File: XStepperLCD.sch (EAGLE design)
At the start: 43 parts, among them Q2 16 MHZ, U1 LCD-16X2NOHOLES

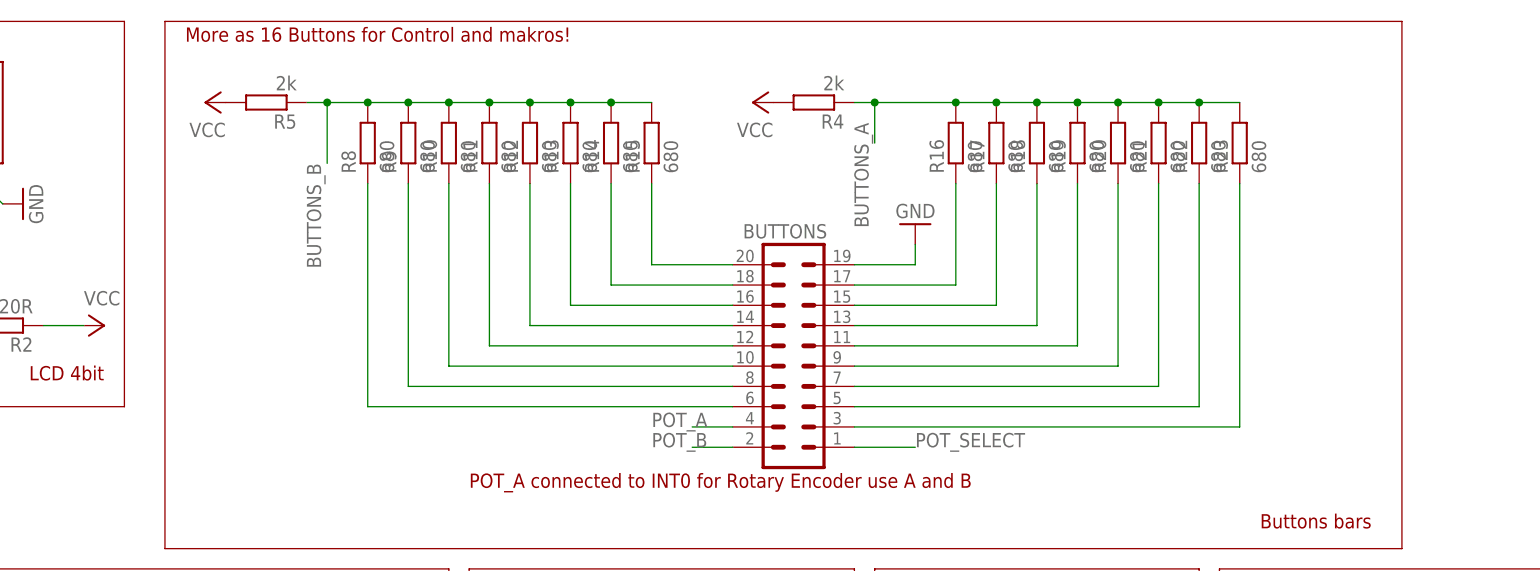
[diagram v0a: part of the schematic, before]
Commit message: - bugfic: set all buttons resistor to different values
- fix schema and board
- fix some typos and bugs in readButtons
- add thread to read buttons
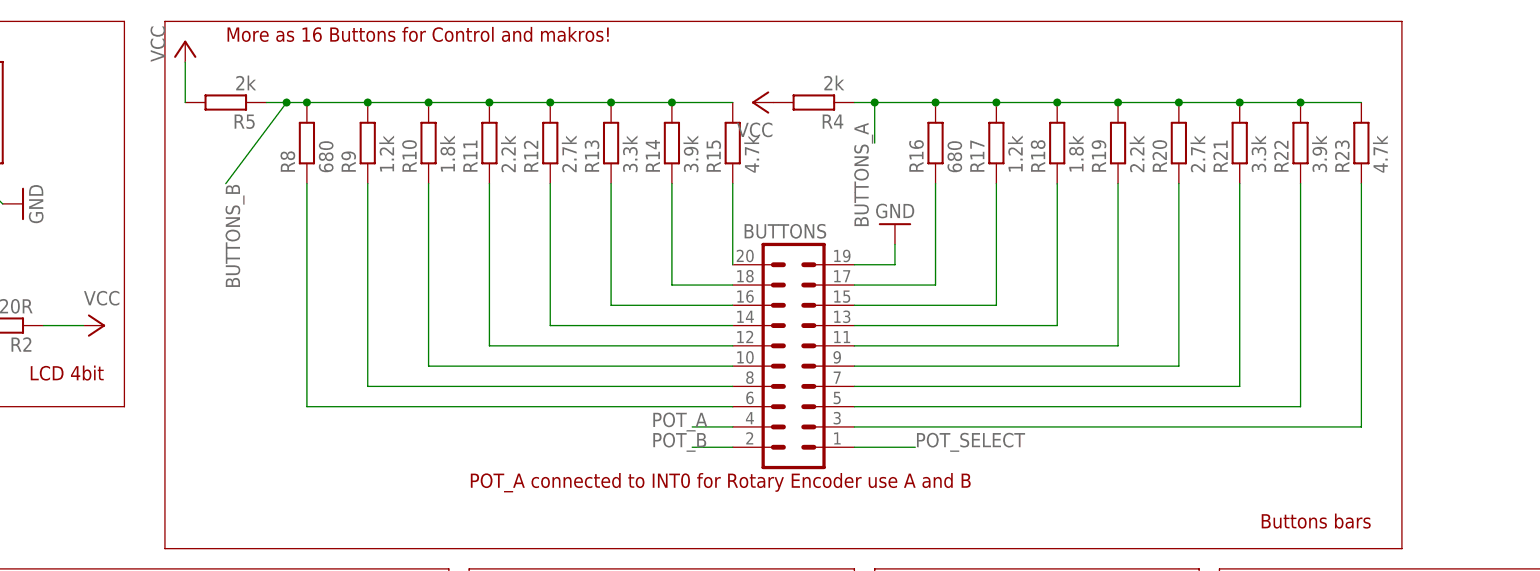
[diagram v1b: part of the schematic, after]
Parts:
- R10, R18: value 680 -> 1.8k
- R11, R19: value 680 -> 2.2k
- R12, R20: value 680 -> 2.7k
- R13, R21: value 680 -> 3.3k
- R14, R22: value 680 -> 3.9k
- R15, R23: value 680 -> 4.7k
- R17, R9: value 680 -> 1.2k
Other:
- moved on the sheet: R10, R12, R13, R14, R15, R16, R18, R19, R20, R21, R22, R23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

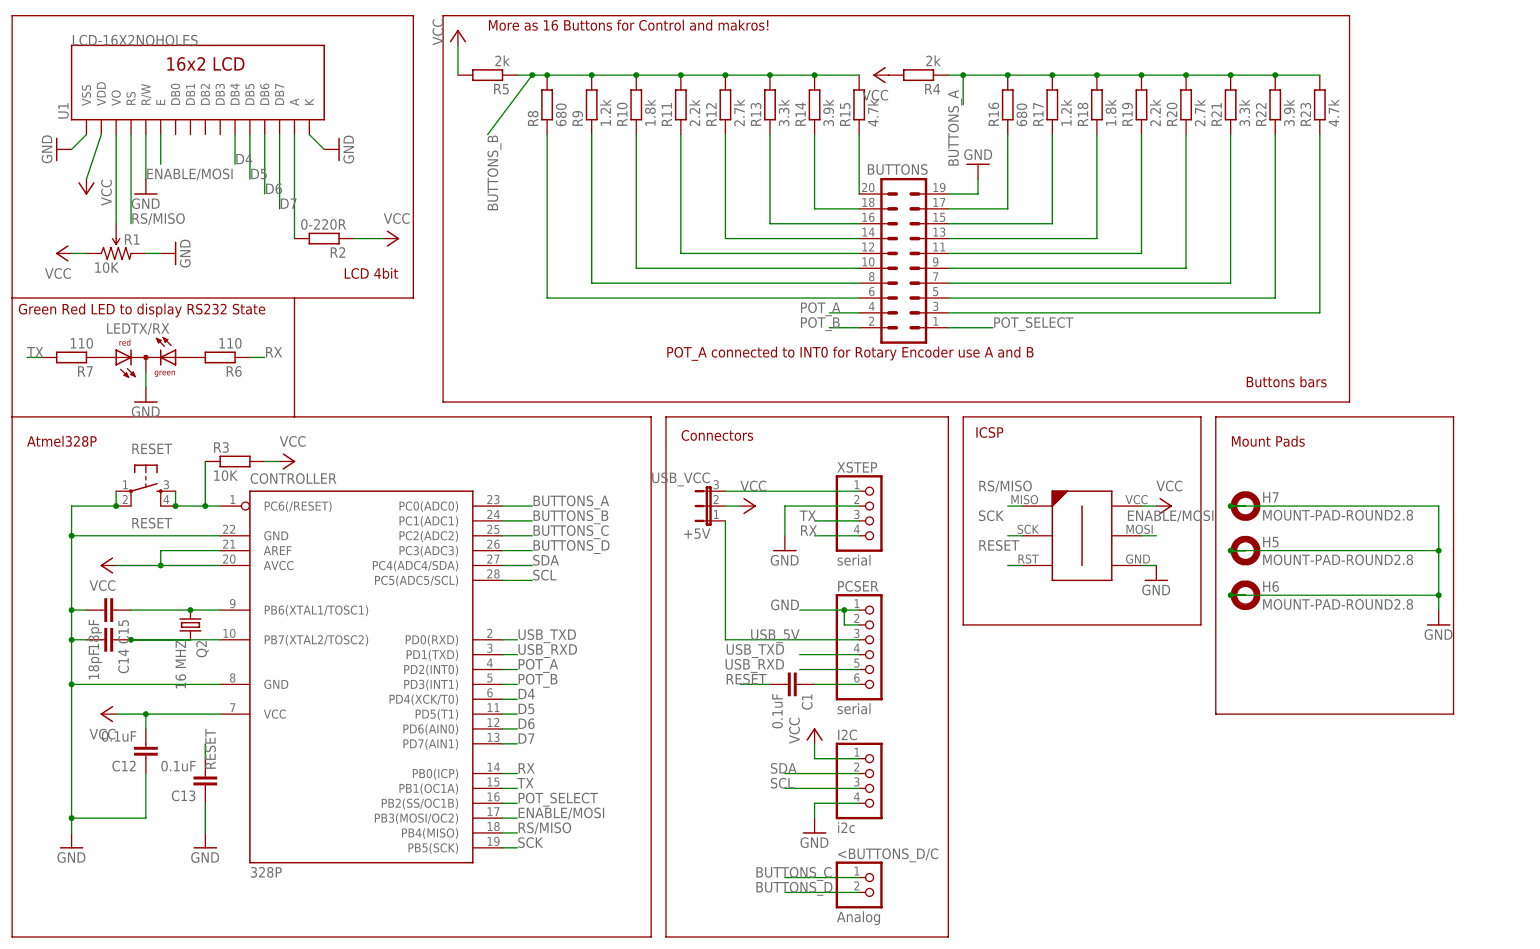
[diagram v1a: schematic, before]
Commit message: - replace some TH parts with SMD and bugfixes
- remove reset button
- remove power pin and choose only power from xstepper
- add RJ45 plugin for connect XStepper
- change all button resistors to 680r and connect serial
- remove LED from serial line and put a new one to A7
- add some text to I2C
- change Atmega328 to SMD Version
- change Quartz to SMD ceramic resonator (16MHz)
- replace ICSP to normal 2x3 pin header
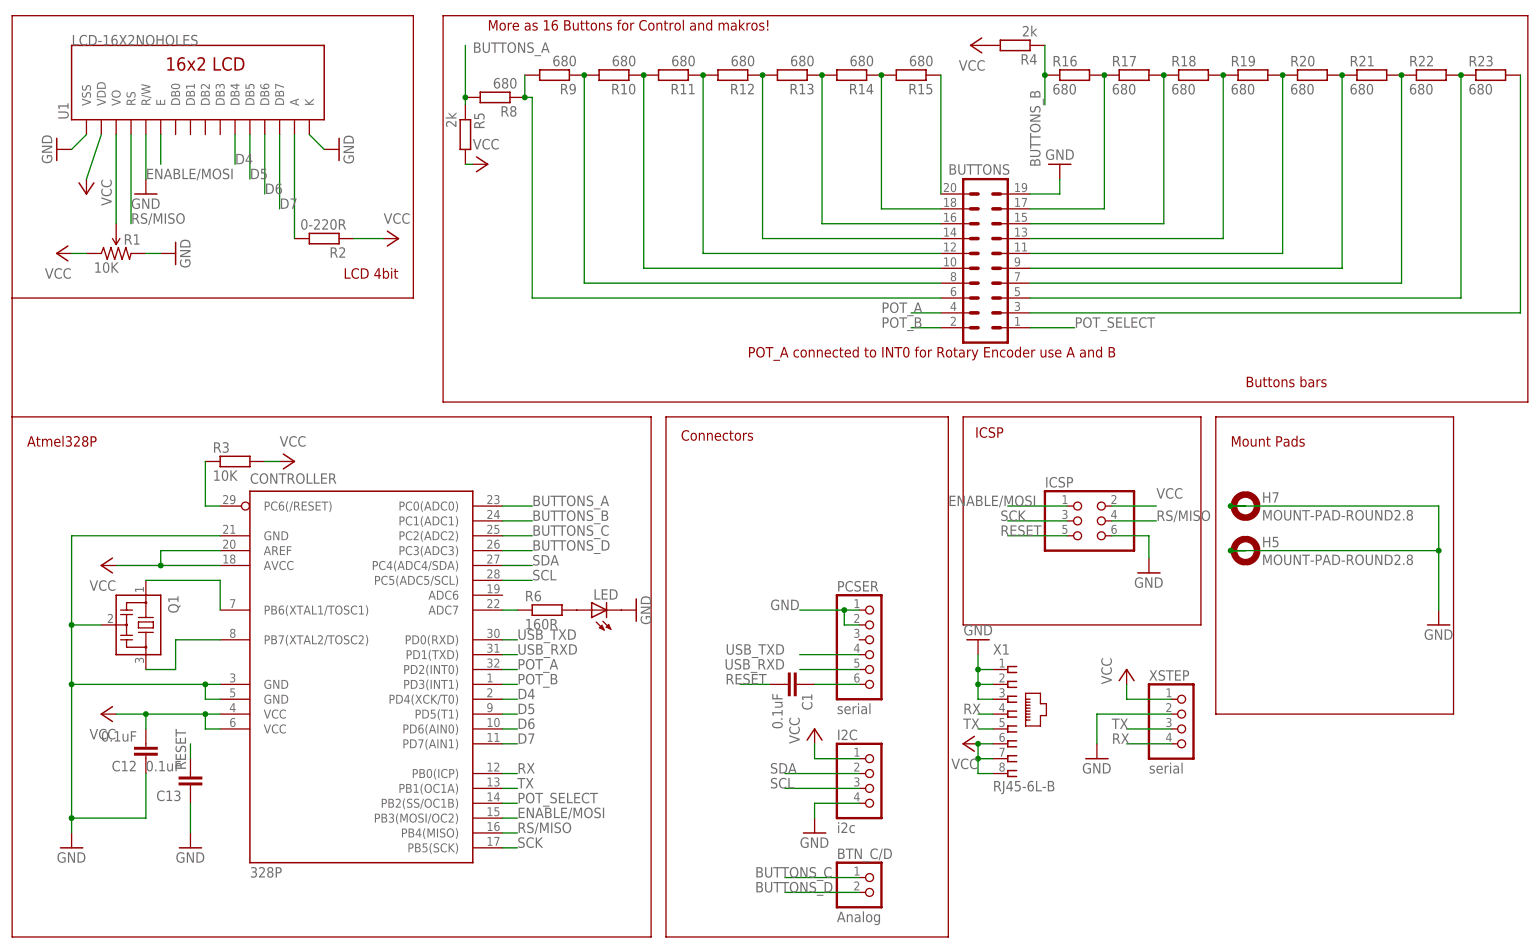
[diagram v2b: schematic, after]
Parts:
- removed +5V: USB_VCC, jumper:JP2E
- removed C14, C15: 18pF, resistor:C-EUC1206
- removed H6: MOUNT-PAD-ROUND2.8, holes:MOUNT-PAD-ROUND2.8
- removed LEDTX/RX: (no value), led:DUOLED2X5
- removed Q2: 16 MHZ, crystal:CRYSTALHC49S
- removed R7: 110, resistor:R-EU_R1206
- removed RESET: RESET, SparkFun:TAC_SWITCHSMD
- added LED: (no value), led:LEDSMT1206
- added Q1: CSTCR6M00G53Z, murata-filter:CSTCR6M00G53Z
- added X1: RJ45-6L-B, con-tycoelectronics:RJ45-6L-B
- 328P: device Bibsatmel:MEGA8-P -> atmel:MEGA8-AI
- ICSP: value ICSP -> (none); device avr-7:AVR-ISP-6-EDGE -> pinhead:PINHD-2X3
- R10, R18: value 1.8k -> 680
- R11, R19: value 2.2k -> 680
- R12, R20: value 2.7k -> 680
- R13, R21: value 3.3k -> 680
- R14, R22: value 3.9k -> 680
- R15, R23: value 4.7k -> 680
- R17, R9: value 1.2k -> 680
- R6: value 110 -> 160R
- renumbered <BUTTONS_D/C to BTN_C/D
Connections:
- removed net N$12 (its old number): BUTTONS.12, R11.1
- removed net N$16: BUTTONS.7, R21.1
- removed net N$17: BUTTONS.9, R20.1
- removed net N$18: BUTTONS.11, R19.1
- removed net N$19: BUTTONS.18, R14.1
- removed net N$21: LEDTX/RX.AG, R6.2
- removed net N$22: LEDTX/RX.AR, R7.1
- removed net N$33: 328P.PB6(XTAL1/TOSC1), C15.1, Q2.1
- removed net USB_5V: +5V.1, PCSER.3
- removed net XSTEP_5V: +5V.3, XSTEP.1
- new net N$23: BUTTONS.17, R16.2, R17.1
- new net N$24: BUTTONS.15, R17.2, R18.1
- new net N$25: BUTTONS.13, R18.2, R19.1
- new net N$26: BUTTONS.11, R19.2, R20.1
- new net N$27: BUTTONS.9, R20.2, R21.1
- new net N$28: BUTTONS.7, R21.2, R22.1
- new net N$29: BUTTONS.5, R22.2, R23.1
- new net N$3: 328P.PB6(XTAL1/TOSC1), Q1.1
- net BUTTONS_A: now also R5.1, R8.2; no longer R16.2, R17.2, R18.2, R19.2, R20.2, R21.2, R22.2, R23.2, R4.1
- net BUTTONS_B: now also R16.1, R4.1; no longer R10.2, R11.2, R12.2, R13.2, R14.2, R15.2, R5.1, R8.2, R9.2
- net ENABLE/MOSI: now also ICSP.1; no longer ICSP.P$5
- net GND: now also 328P.GND@2, ICSP.6, LED.C, Q1.2, X1.1, X1.2, X1.3; no longer C14.2, C15.2, H6.MOUNT, ICSP.P$4, LEDTX/RX.C, RESET.1, RESET.2
- net N$10: now also BUTTONS.18, R14.1, R15.2; no longer BUTTONS.5, R22.1
- net N$11: now also BUTTONS.14, R12.1, R13.2; no longer BUTTONS.10, R10.1
- net N$13: now also LED.A, R6.2; no longer BUTTONS.14, R12.1
- net N$15: now also 328P.ADC7, R6.1; no longer BUTTONS.16, R13.1
- net N$34: now also Q1.3; no longer C14.1, Q2.2
- net N$4: now also BUTTONS.3, R23.2; no longer BUTTONS.13, R18.1
- net N$5: now also BUTTONS.6, R8.1, R9.2; no longer BUTTONS.15, R17.1
- net N$6: now also BUTTONS.8, R10.2, R9.1; no longer BUTTONS.17, R16.1
- net N$7: now also BUTTONS.10, R10.1, R11.2; no longer BUTTONS.6, R8.1
- net N$8: now also BUTTONS.12, R11.1, R12.2; no longer BUTTONS.8, R9.1
- net N$9: now also BUTTONS.16, R13.1, R14.2; no longer BUTTONS.3, R23.1
- net RESET: now also ICSP.5; no longer ICSP.P$3, RESET.3, RESET.4
- net RS/MISO: now also ICSP.4; no longer ICSP.P$1
- net RX: now also X1.4; no longer R6.1
- net SCK: now also ICSP.3; no longer ICSP.P$2
- net TX: now also X1.5; no longer R7.2
- net VCC: now also 328P.VCC@2, ICSP.2, X1.6, X1.7, X1.8, XSTEP.1; no longer +5V.2, ICSP.P$6
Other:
- note removed: "Green Red LED to display RS232 State"
- moved on the sheet: BUTTONS, C13, R10, R11, R12, R13, R14, R15, R16, R17, R18, R19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

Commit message: make board bigger
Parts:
- added H1, H2: MOUNT-PAD-ROUND2.8, holes:MOUNT-PAD-ROUND2.8
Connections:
- net BUTTONS_C: now also 328P.ADC6; no longer 328P.PC2(ADC2)
- net BUTTONS_D: now also 328P.ADC7; no longer 328P.PC3(ADC3)
- net ENABLE/MOSI: now also ICSP.4; no longer ICSP.1
- net N$15: now also 328P.PC2(ADC2); no longer 328P.ADC7
- net RS/MISO: now also ICSP.1; no longer ICSP.4
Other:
- moved on the sheet: LED, R6
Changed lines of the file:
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@@
 <?xml version="1.0" encoding="utf-8"?>
 <!DOCTYPE eagle SYSTEM "eagle.dtd">
-<eagle version="6.5.0">
+<eagle version="6.3">
 <drawing>
 <settings>
@@
 <part name="GND11" library="supply1" deviceset="GND" device=""/>
 <part name="P+2" library="supply1" deviceset="VCC" device=""/>
+<part name="H1" library="holes" deviceset="MOUNT-PAD-ROUND" device="2.8" value="MOUNT-PAD-ROUND2.8"/>
+<part name="H2" library="holes" deviceset="MOUNT-PAD-ROUND" device="2.8" value="MOUNT-PAD-ROUND2.8"/>
 </parts>
 <sheets>
@@
 <instance part="GND5" gate="1" x="191.77" y="11.43"/>
 <instance part="Q1" gate="G$1" x="20.32" y="2.54" rot="R270"/>
-<instance part="LED" gate="G$1" x="96.52" y="5.08" rot="R90"/>
-<instance part="GND9" gate="1" x="104.14" y="5.08" rot="R90"/>
-<instance part="R6" gate="G$1" x="88.9" y="5.08"/>
+<instance part="LED" gate="G$1" x="96.52" y="17.78" rot="R90"/>
+<instance part="GND9" gate="1" x="104.14" y="17.78" rot="R90"/>
+<instance part="R6" gate="G$1" x="88.9" y="17.78"/>
 <instance part="X1" gate="G$1" x="167.64" y="-12.7"/>
 <instance part="GND11" gate="1" x="162.56" y="0" rot="R180"/>
 <instance part="P+2" gate="VCC" x="160.02" y="-17.78" rot="R90"/>
+<instance part="H1" gate="G$1" x="208.28" y="7.62"/>
+<instance part="H2" gate="G$1" x="208.28" y="30.48"/>
 </instances>
 <busses>
@@
 <wire x1="205.74" y1="15.24" x2="241.3" y2="15.24" width="0.1524" layer="91"/>
 <wire x1="241.3" y1="15.24" x2="241.3" y2="22.86" width="0.1524" layer="91"/>
-<wire x1="241.3" y1="5.08" x2="241.3" y2="15.24" width="0.1524" layer="91"/>
+<wire x1="241.3" y1="5.08" x2="241.3" y2="7.62" width="0.1524" layer="91"/>
 <junction x="241.3" y="15.24"/>
 <pinref part="GND24" gate="1" pin="GND"/>
@@
 <pinref part="H5" gate="G$1" pin="MOUNT"/>
 <junction x="205.74" y="15.24"/>
+<wire x1="241.3" y1="7.62" x2="241.3" y2="15.24" width="0.1524" layer="91"/>
+<wire x1="208.28" y1="30.48" x2="241.3" y2="30.48" width="0.1524" layer="91"/>
+<wire x1="241.3" y1="30.48" x2="241.3" y2="22.86" width="0.1524" layer="91"/>
+<junction x="241.3" y="22.86"/>
+<wire x1="208.28" y1="7.62" x2="241.3" y2="7.62" width="0.1524" layer="91"/>
+<junction x="241.3" y="7.62"/>
 </segment>
 <segment>
@@
 </segment>
 <segment>
-<pinref part="ICSP" gate="A" pin="4"/>
-<wire x1="185.42" y1="20.32" x2="193.04" y2="20.32" width="0.1524" layer="91"/>
-<label x="193.04" y="20.32" size="1.778" layer="95"/>
+<pinref part="ICSP" gate="A" pin="1"/>
+<wire x1="177.8" y1="22.86" x2="167.64" y2="22.86" width="0.1524" layer="91"/>
+<label x="157.48" y="22.86" size="1.778" layer="95"/>
 </segment>
 </net>
@@
 </segment>
 <segment>
-<pinref part="ICSP" gate="A" pin="1"/>
-<wire x1="177.8" y1="22.86" x2="167.64" y2="22.86" width="0.1524" layer="91"/>
-<label x="157.48" y="22.86" size="1.778" layer="95"/>
+<pinref part="ICSP" gate="A" pin="4"/>
+<wire x1="185.42" y1="20.32" x2="193.04" y2="20.32" width="0.1524" layer="91"/>
+<label x="193.04" y="20.32" size="1.778" layer="95"/>
 </segment>
 </net>
 <net name="BUTTONS_C" class="0">
-<segment>
-<pinref part="328P" gate="G$1" pin="PC2(ADC2)"/>
-<wire x1="81.28" y1="17.78" x2="86.36" y2="17.78" width="0.1524" layer="91"/>
-<label x="86.36" y="17.78" size="1.778" layer="95"/>
-</segment>
 <segment>
 <pinref part="BTN_C/D" gate="G$1" pin="1"/>
@@
 <label x="124.46" y="-40.64" size="1.778" layer="95"/>
 </segment>
+<segment>
+<pinref part="328P" gate="G$1" pin="ADC6"/>
+<wire x1="81.28" y1="7.62" x2="86.36" y2="7.62" width="0.1524" layer="91"/>
+<label x="86.36" y="7.62" size="1.778" layer="95"/>
+</segment>
 </net>
 <net name="BUTTONS_D" class="0">
-<segment>
-<pinref part="328P" gate="G$1" pin="PC3(ADC3)"/>
-<wire x1="81.28" y1="15.24" x2="86.36" y2="15.24" width="0.1524" layer="91"/>
-<label x="86.36" y="15.24" size="1.778" layer="95"/>
-</segment>
 <segment>
 <pinref part="BTN_C/D" gate="G$1" pin="2"/>
 <wire x1="142.24" y1="-43.18" x2="129.54" y2="-43.18" width="0.1524" layer="91"/>
 <label x="124.46" y="-43.18" size="1.778" layer="95"/>
+</segment>
+<segment>
+<pinref part="328P" gate="G$1" pin="ADC7"/>
+<wire x1="81.28" y1="5.08" x2="86.36" y2="5.08" width="0.1524" layer="91"/>
+<label x="86.36" y="5.08" size="1.778" layer="95"/>
 </segment>
 </net>
@@
 <net name="N$15" class="0">
 <segment>
-<pinref part="328P" gate="G$1" pin="ADC7"/>
+<pinref part="328P" gate="G$1" pin="PC2(ADC2)"/>
 <pinref part="R6" gate="G$1" pin="1"/>
-<wire x1="81.28" y1="5.08" x2="83.82" y2="5.08" width="0.1524" layer="91"/>
-</segment>
-</net>
+<wire x1="81.28" y1="17.78" x2="83.82" y2="17.78" width="0.1524" layer="91"/>
+</segment>
+</net>
